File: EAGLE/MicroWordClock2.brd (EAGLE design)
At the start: 20.3 x 20.3 mm, 20 parts, among them IC1 ATMEGA328P, IC2 DS1307SMD

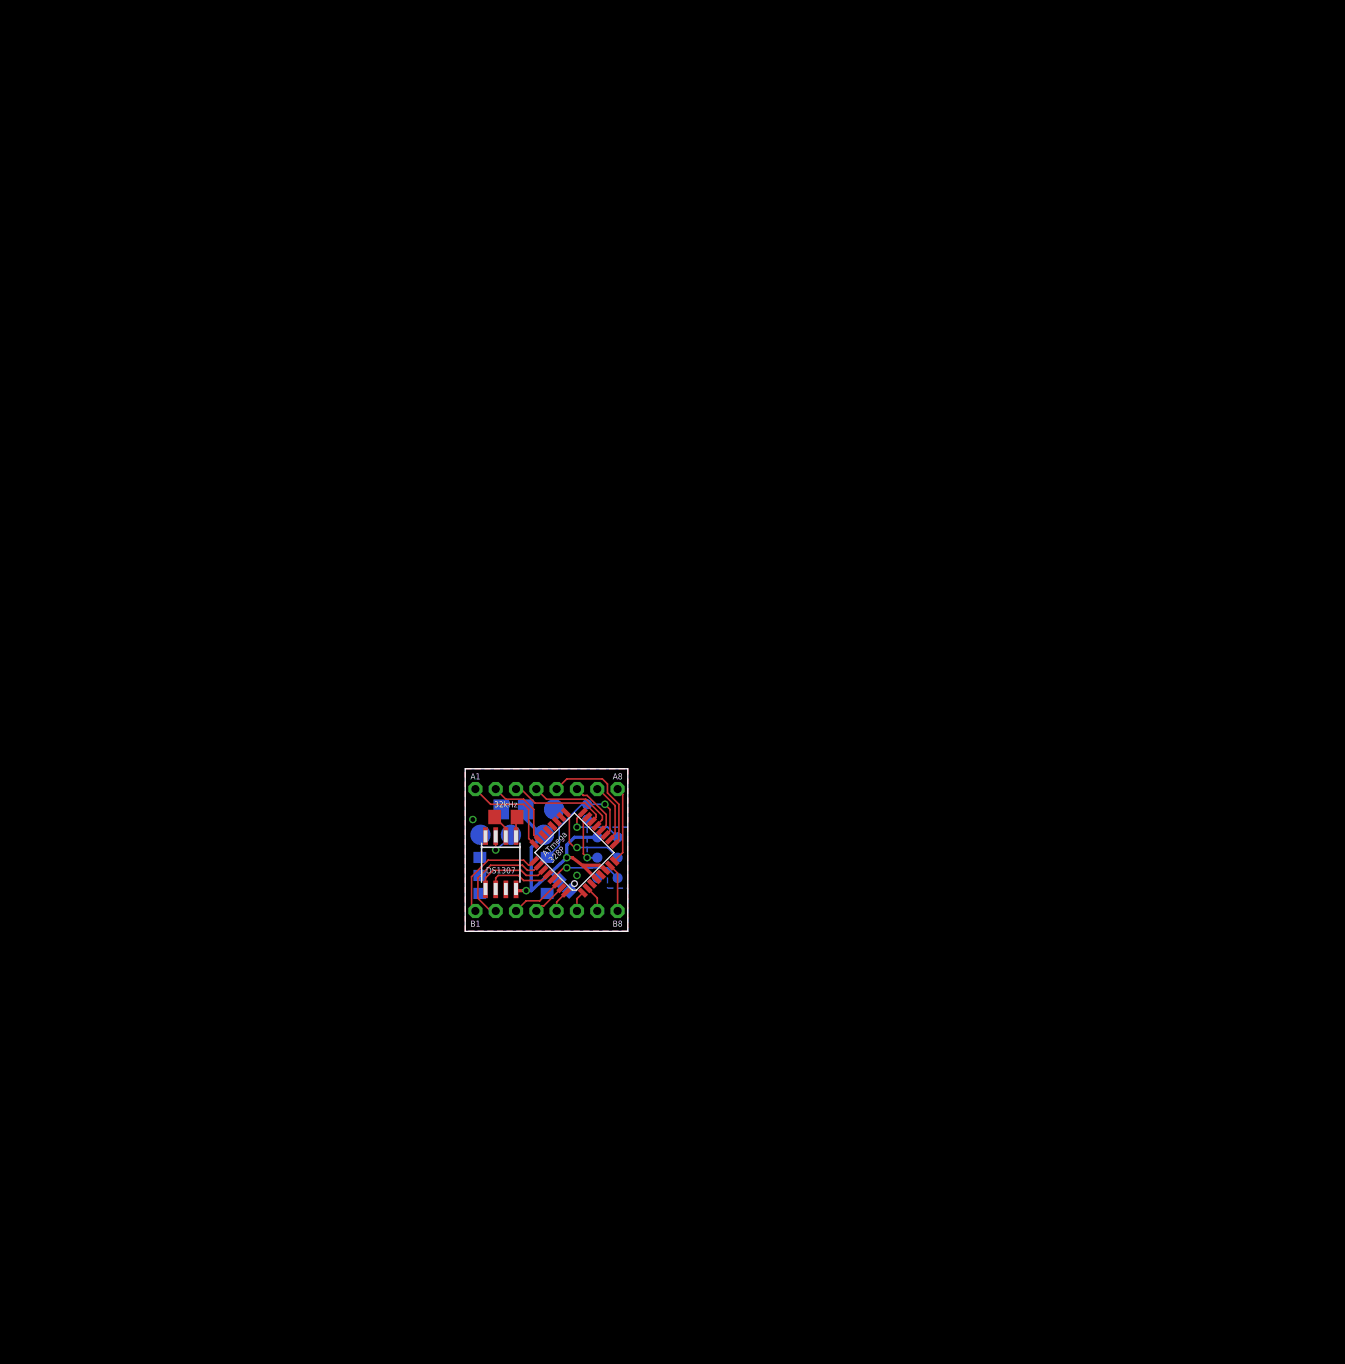
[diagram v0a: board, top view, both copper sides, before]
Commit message: initial edits to update the existing layout with the same components as the original
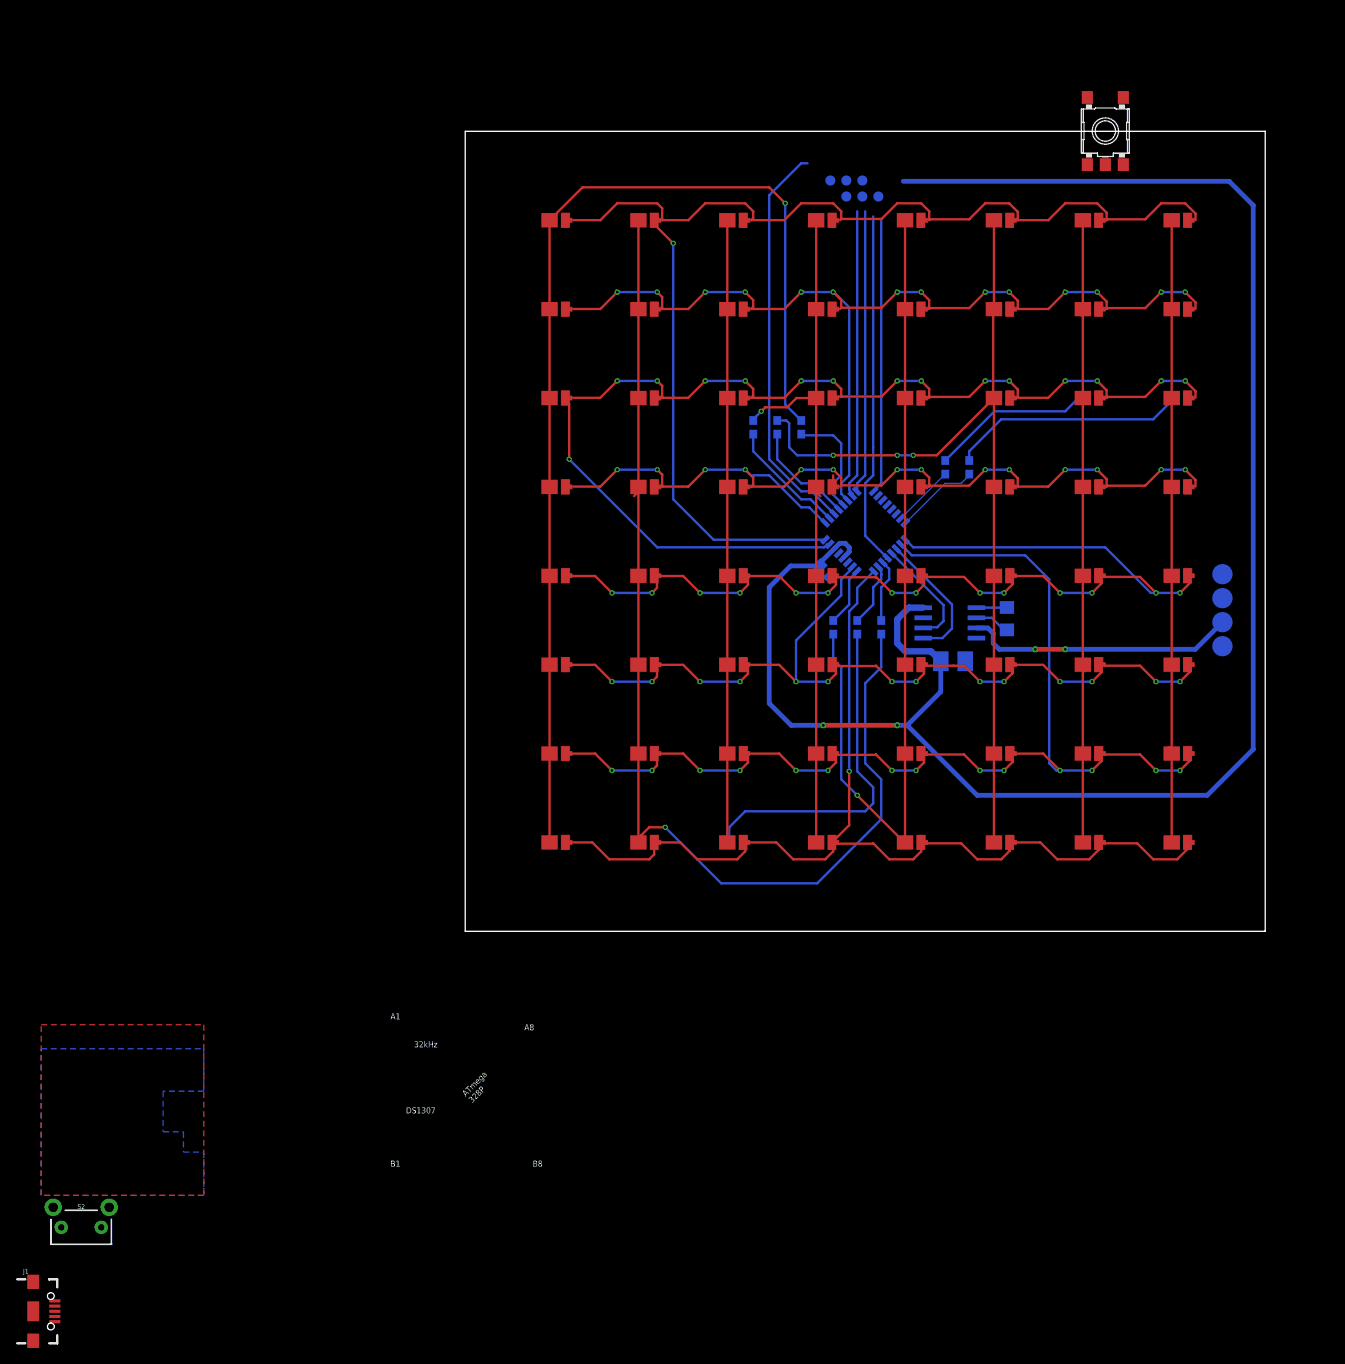
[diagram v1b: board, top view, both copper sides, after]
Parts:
- removed JP_A, JP_B: (no value), adafruit:1X08-CLEANBIG
- removed TP_SWITCH, TP_SWITCH_GND: TPB1,27, testpad:B1,27
- added J1: (no value), SparkFun-Connectors:USB-AB-MICRO-SMD
- added R1, R2, R3, R4, R5, R6, R7, R8: 470, SparkFun-Resistors:0603
- added S2: MOMENTARY-SWITCH-SPST-PTH-RIGHT-ANGLE-KIT, SparkFun-Switches:TACTILE_SWITCH_PTH_RIGHT_ANGLE_KIT
- added U$1, U$10, U$11, U$12, U$13, U$14, U$15, U$16, U$17, U$18, U$19, U$2, U$20, U$21, U$22, U$23, U$24, U$25, U$26, U$27, U$28, U$29, U$3, U$30, U$31, U$32, U$33, U$34, U$35, U$36, U$37, U$38, U$39, U$4, U$40, U$41, U$42, U$43, U$44, U$45, U$46, U$47, U$48, U$49, U$5, U$50, U$51, U$52, U$53, U$54, U$55, U$56, U$57, U$58, U$59, U$6, U$60, U$61, U$62, U$63, U$64, U$7, U$8, U$9: (no value), TULIP_GIZMO:1113(2835METRIC)
- moved S1 118.9 mm to (80.0, 100.0), flipped to the top, turned to 270 degrees
- moved TP_BAT- 95.7 mm to (94.7, 35.6), turned to 270 degrees
- moved TP_BAT+ 92.8 mm to (94.7, 38.6), turned to 270 degrees
- moved TP_GND 92.6 mm to (47.6, 93.8)
- moved TP_RST 89.9 mm to (47.6, 91.8)
- moved TP_VCC1 89.8 mm to (94.7, 41.6), turned to 270 degrees
- moved TP_MOSI 89.5 mm to (45.6, 93.8)
- moved TP_SCK 88.8 mm to (51.6, 91.8)
- moved TP_GND1 88.6 mm to (94.7, 44.6), turned to 270 degrees
- moved TP_MISO 87.6 mm to (49.6, 93.8)
- moved TP_VCC 86.7 mm to (49.6, 91.8)
- moved XTAL 67.4 mm to (67.7, 39.1), flipped to the bottom, turned to 90 degrees
- moved IC2 63.6 mm to (60.6, 38.6), flipped to the bottom, turned to 270 degrees
- moved C2 58.0 mm to (61.0, 33.8), turned to 0 degrees
- moved IC1 54.2 mm to (50.0, 50.0), flipped to the bottom
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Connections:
- removed net A1: IC1.24, JP_A.1
- removed net A2: IC1.23, JP_A.2
- removed net A3: IC1.14, JP_A.3
- removed net A4: IC1.13, JP_A.4
- removed net A5: IC1.9, JP_A.5
- removed net A6: IC1.12, JP_A.6
- removed net A7: IC1.10, JP_A.7
- removed net A8: IC1.8, JP_A.8
- removed net B1: IC1.25, JP_B.1
- removed net B2: IC1.26, JP_B.2
- removed net B3: IC1.30, JP_B.3
- removed net B4: IC1.31, JP_B.4
- removed net B5: IC1.32, JP_B.5
- removed net B6: IC1.1, JP_B.6
- removed net B7: IC1.2, JP_B.7
- removed net B8: IC1.7, JP_B.8
- new net COL1: IC1.13, R1.1
- new net COL2: IC1.30, R2.1
- new net COL3: IC1.31, R3.1
- new net COL4: IC1.10, R4.1
- new net COL5: IC1.1, R5.1
- new net COL6: IC1.12, R6.1
- new net COL7: IC1.23, R7.1
- new net COL8: IC1.24, R8.1
- new net EE: R8.2, U$57.CATHODE, U$58.CATHODE, U$59.CATHODE, U$60.CATHODE, U$61.CATHODE, U$62.CATHODE, U$63.CATHODE, U$64.CATHODE
- new net N$1: S1.1
- new net N$11: R1.2, U$1.CATHODE, U$2.CATHODE, U$3.CATHODE, U$4.CATHODE, U$5.CATHODE, U$6.CATHODE, U$7.CATHODE, U$8.CATHODE
- new net N$15: R2.2, U$10.CATHODE, U$11.CATHODE, U$12.CATHODE, U$13.CATHODE, U$14.CATHODE, U$15.CATHODE, U$16.CATHODE, U$9.CATHODE
- new net N$5: R3.2, U$17.CATHODE, U$18.CATHODE, U$19.CATHODE, U$20.CATHODE, U$21.CATHODE, U$22.CATHODE, U$23.CATHODE, U$24.CATHODE
- new net N$6: R4.2, U$25.CATHODE, U$26.CATHODE, U$27.CATHODE, U$28.CATHODE, U$29.CATHODE, U$30.CATHODE, U$31.CATHODE, U$32.CATHODE
- new net N$7: R5.2, U$33.CATHODE, U$34.CATHODE, U$35.CATHODE, U$36.CATHODE, U$37.CATHODE, U$38.CATHODE, U$39.CATHODE, U$40.CATHODE
- new net N$8: R6.2, U$41.CATHODE, U$42.CATHODE, U$43.CATHODE, U$44.CATHODE, U$45.CATHODE, U$46.CATHODE, U$47.CATHODE, U$48.CATHODE
- new net N$9: R7.2, U$49.CATHODE, U$50.CATHODE, U$51.CATHODE, U$52.CATHODE, U$53.CATHODE, U$54.CATHODE, U$55.CATHODE, U$56.CATHODE
- new net ROW1: IC1.8, U$1.ANODE, U$17.ANODE, U$25.ANODE, U$33.ANODE, U$41.ANODE, U$49.ANODE, U$57.ANODE, U$9.ANODE
- new net ROW2: IC1.14, U$10.ANODE, U$18.ANODE, U$2.ANODE, U$26.ANODE, U$34.ANODE, U$42.ANODE, U$50.ANODE, U$58.ANODE
- new net ROW3: IC1.7, U$11.ANODE, U$19.ANODE, U$27.ANODE, U$3.ANODE, U$35.ANODE, U$43.ANODE, U$51.ANODE, U$59.ANODE
- new net ROW4: IC1.9, U$12.ANODE, U$20.ANODE, U$28.ANODE, U$36.ANODE, U$4.ANODE, U$44.ANODE, U$52.ANODE, U$60.ANODE
- new net ROW5: IC1.25, U$13.ANODE, U$21.ANODE, U$29.ANODE, U$37.ANODE, U$45.ANODE, U$5.ANODE, U$53.ANODE, U$61.ANODE
- new net ROW6: IC1.2, U$14.ANODE, U$22.ANODE, U$30.ANODE, U$38.ANODE, U$46.ANODE, U$54.ANODE, U$6.ANODE, U$62.ANODE
- new net ROW7: IC1.26, U$15.ANODE, U$23.ANODE, U$31.ANODE, U$39.ANODE, U$47.ANODE, U$55.ANODE, U$63.ANODE, U$7.ANODE
- new net ROW8: IC1.32, U$16.ANODE, U$24.ANODE, U$32.ANODE, U$40.ANODE, U$48.ANODE, U$56.ANODE, U$64.ANODE, U$8.ANODE
- new net VBUS: J1.VBUS1
- net GND: now also J1.GND1, J1.SHLD1, J1.SHLD2, J1.SHLD3; no longer TP_SWITCH_GND.TP
- net SWITCH: no longer S1.1, TP_SWITCH.TP
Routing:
- net +5V: track 37.0 -> 232.4 mm
- net ROW1: track 0.00 -> 150.8 mm, vias 0 -> 1
- net N$15: track 0.00 -> 142.4 mm, vias 0 -> 1
- net ROW3: track 0.00 -> 140.1 mm, vias 0 -> 15
- net ROW7: track 0.00 -> 140.0 mm, vias 0 -> 14
- net N$11: track 0.00 -> 137.8 mm, vias 0 -> 1
- net ROW8: track 0.00 -> 131.0 mm, vias 0 -> 1
- net ROW5: track 0.00 -> 129.0 mm, vias 0 -> 14
- net ROW2: track 0.00 -> 122.5 mm, vias 0 -> 14
- net N$5: track 0.00 -> 122.3 mm
- net ROW6: track 0.00 -> 112.1 mm, vias 0 -> 14
- net N$8: track 0.00 -> 110.5 mm, vias 0 -> 3
- net ROW4: track 0.00 -> 109.1 mm, vias 0 -> 14
- net EE: track 0.00 -> 108.7 mm
- net N$7: track 0.00 -> 107.2 mm, vias 0 -> 1
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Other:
- board size 20.3 x 20.3 mm -> 100 x 100 mm

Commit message: board with new footprints for switch, microusb and clock & complete routing
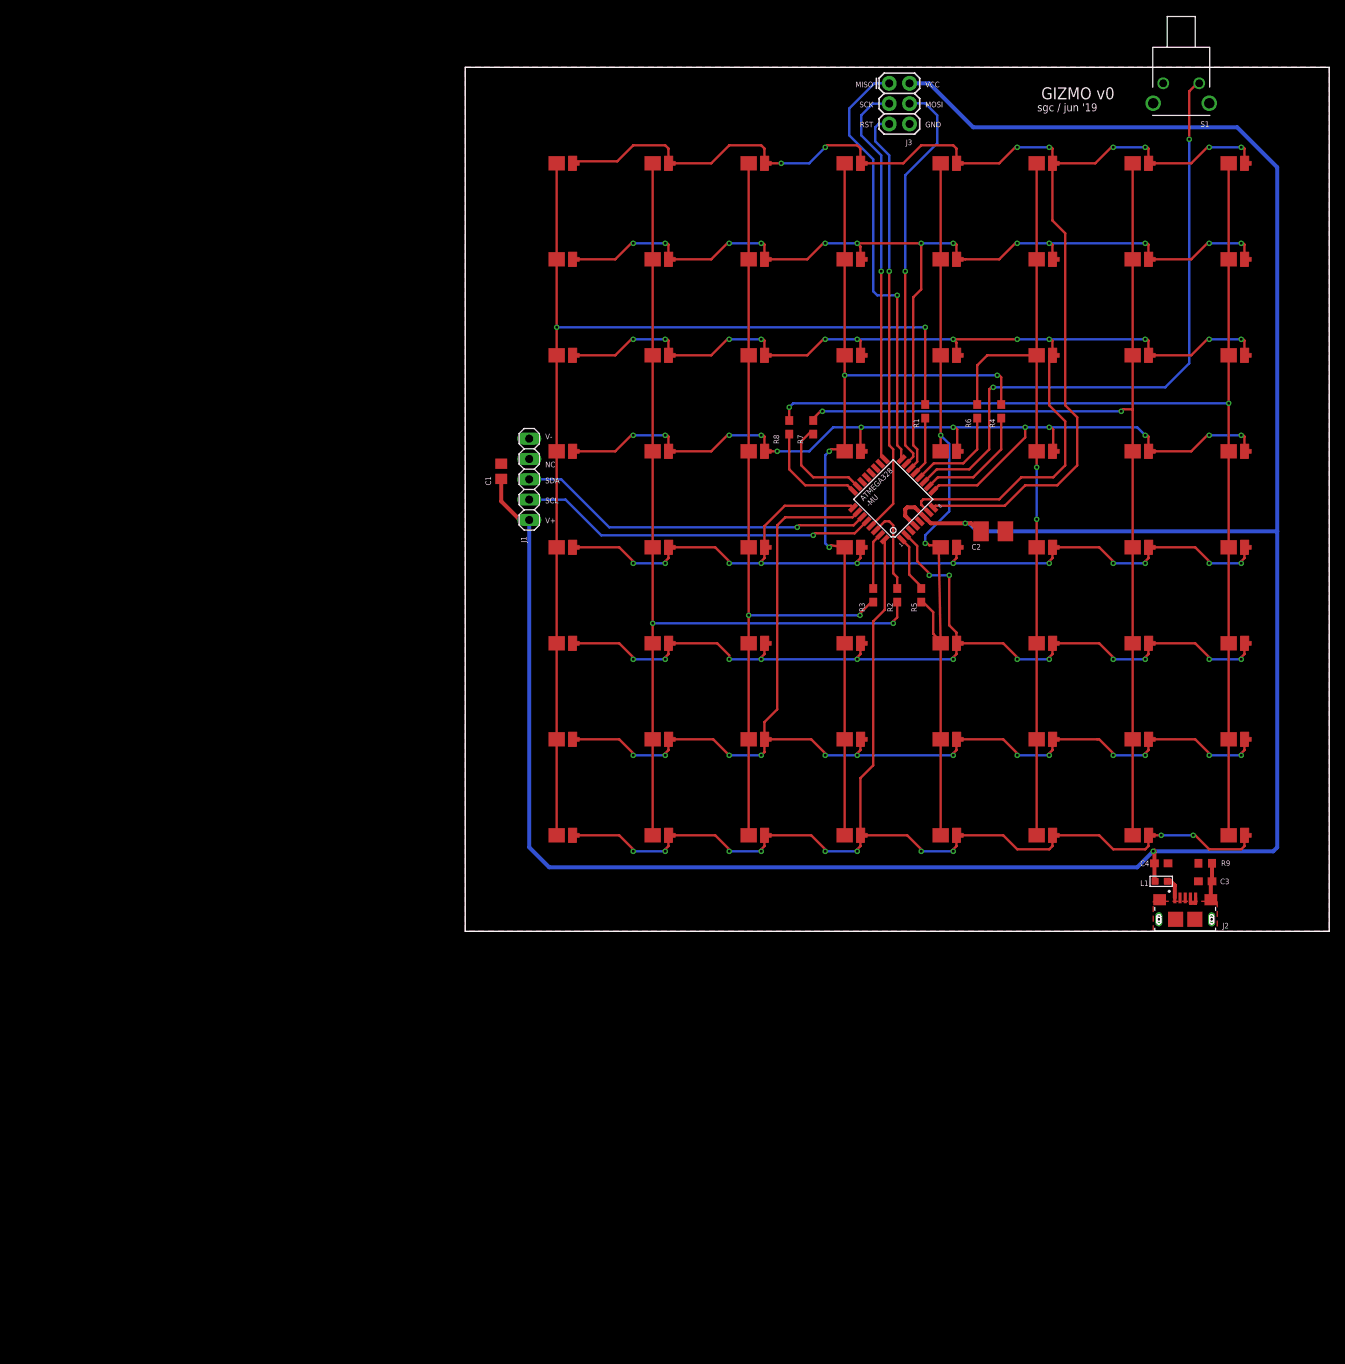
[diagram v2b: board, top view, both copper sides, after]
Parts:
- removed IC1: ATMEGA328P, atmel:TQFP32-08
- removed IC2: DS1307SMD, DS1307:SO-08M
- removed S2: MOMENTARY-SWITCH-SPST-PTH-RIGHT-ANGLE-KIT, SparkFun-Switches:TACTILE_SWITCH_PTH_RIGHT_ANGLE_KIT
- removed TP_BAT+, TP_BAT-, TP_GND1, TP_VCC1: TPB2,54, testpad:B2,54
- removed TP_GND, TP_MISO, TP_MOSI, TP_RST, TP_SCK, TP_VCC: TPB1,27, testpad:B1,27
- removed XTAL: XTAL-32KHZ, xtal-32khz:XTAL-SMD-1206-3216M
- added C3: 4700pF, rcl:C0603
- added C4: 4.7uF, rcl:C0603
- added J2: 10118193-0001LF, 10118193-0001LF:FCI_10118193-0001LF
- added J3: AVR_SPI_PROG_3X2PTH, SparkFun-Connectors:2X3
- added L1: 120OHM-500MA, OPL_Ferrite_and_Magnetic_Bead:L0603
- added R9: 10M, rcl:R0603
- added U1: ATMEGA328P, atmel:TQFP32-08
- J1: value (none) -> DS3231S#T&RMODULE; device SparkFun-Connectors:USB-AB-MICRO-SMD -> DS3231:1X05
- S1: value SKHMPSE010 -> 1-1825027-1; device switch:SKHMPXE010 -> 1-1825027-1:SW_1-1825027-1
- moved J1 121.1 mm to (8.00, 56.5), turned to 90 degrees
- moved C1 42.4 mm to (4.50, 57.5), flipped to the top, turned to 90 degrees
- moved R4 31.1 mm to (67.0, 65.0), flipped to the top
- moved R6 25.1 mm to (64.0, 65.0), flipped to the top
- moved R8 23.0 mm to (40.5, 63.0), flipped to the top
- moved R7 17.2 mm to (43.5, 63.0), flipped to the top
- moved C2 17.0 mm to (66.0, 50.0), flipped to the top, turned to 180 degrees
- moved R1 15.6 mm to (57.5, 65.0), flipped to the top
- moved R5 11.7 mm to (57.0, 42.0), flipped to the top
- moved S1 11.2 mm to (89.5, 106.0), turned to 180 degrees
- moved U$57 10.1 mm to (96.0, 96.0)
- moved U$49 9.46 mm to (84.0, 96.0)
- moved U$58 9.46 mm to (96.0, 84.0)
- moved U$41 8.90 mm to (72.0, 96.0)
- moved U$59 8.90 mm to (96.0, 72.0)
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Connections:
- removed net N$14: IC2.1, XTAL.X2
- removed net N$18: IC1.28, IC2.6
- removed net N$2: IC2.2, XTAL.X1
- removed net SWITCH: IC1.11
- removed net VBAT: IC2.3, TP_BAT+.TP
- removed net VBUS: J1.VBUS1
- new net PE: C3.2, J2.S1, J2.S2, J2.S3, J2.S4, J2.S5, J2.S6, R9.1
- new net SCL: J1.2, U1.28
- new net V_USB: J2.1, L1.1
- net +5V: now also C4.1, J1.1, J3.2, L1.2, U1.4, U1.6; no longer IC1.4, IC1.6, IC2.8, TP_VCC.TP, TP_VCC1.TP
- net AVCC: now also U1.18; no longer IC1.18
- net COL1: now also U1.13; no longer IC1.13
- net COL2: now also U1.30; no longer IC1.30
- net COL3: now also U1.31; no longer IC1.31
- net COL4: now also U1.10; no longer IC1.10
- net COL5: now also U1.1; no longer IC1.1
- net COL6: now also U1.12; no longer IC1.12
- net COL7: now also U1.23; no longer IC1.23
- net COL8: now also U1.24; no longer IC1.24
- net GND: now also C3.1, C4.2, J1.5, J2.4, J2.5, J3.6, R9.2, S1.2, S1.S1, S1.S2, U1.21, U1.3, U1.5; no longer IC1.21, IC1.3, IC1.5, IC2.4, J1.GND1, J1.SHLD1, J1.SHLD2, J1.SHLD3, S1.3, S1.4, S1.5, TP_BAT-.TP, TP_GND.TP, TP_GND1.TP
- net MISO: now also J3.1, U1.16; no longer IC1.16, TP_MISO.TP
- net MOSI: now also J3.4, U1.15; no longer IC1.15, TP_MOSI.TP
- net N$1: now also U1.11
- net RESET: now also J3.5, U1.29; no longer IC1.29, TP_RST.TP
- net ROW1: now also U1.8; no longer IC1.8
- net ROW2: now also U1.14; no longer IC1.14
- net ROW3: now also U1.7; no longer IC1.7
- net ROW4: now also U1.9; no longer IC1.9
- net ROW5: now also U1.25; no longer IC1.25
- net ROW6: now also U1.2; no longer IC1.2
- net ROW7: now also U1.26; no longer IC1.26
- net ROW8: now also U1.32; no longer IC1.32
- net SCK: now also J3.3, U1.17; no longer IC1.17, TP_SCK.TP
- net SDA: now also J1.3, U1.27; no longer IC1.27, IC2.5
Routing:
- net +5V: track 232.4 -> 336.0 mm
- net N$1: track 0.00 -> 79.3 mm, vias 0 -> 2
- net SWITCH: track 50.4 -> 0.00 mm
- net SCL: track 0.00 -> 44.8 mm, vias 0 -> 1
- net VBAT: track 34.0 -> 0.00 mm, vias 2 -> 0
- net EE: track 108.7 -> 140.8 mm, vias 0 -> 2
- net SDA: track 17.0 -> 44.6 mm, vias 0 -> 1
- net N$15: track 142.4 -> 116.9 mm, vias 1 -> 2
- net N$9: track 100.6 -> 124.7 mm, vias 0 -> 2
- net N$6: track 88.2 -> 111.3 mm, vias 1 -> 4
- net N$5: track 122.3 -> 100.4 mm, vias 0 -> 2
- net MISO: track 35.4 -> 54.3 mm, vias 0 -> 1
- net MOSI: track 36.1 -> 50.1 mm, vias 0 -> 1
- net SCK: track 34.4 -> 48.3 mm, vias 0 -> 1
- net N$8: track 110.5 -> 96.8 mm, vias 3 -> 2
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- added copper zone on layer 1, net PE
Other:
- board size 100 x 100 mm -> 108 x 108 mm
- board text added: "1"
- board text added: "8"
- board text added: "ATMEGA328 -MU"
- board text added: "GIZMO v0"
- board text added: "MISO"
- board text added: "MOSI"
- board text added: "NC"
- board text added: "RST"
- board text added: "SCK"
- board text added: "SCL"
- board text added: "SDA"
- board text added: "V+"
- board text added: "V-"
- board text added: "sgc / jun '19"
- board text removed: "+"
- board text removed: "-"
- board text removed: "2.2 uF"
- board text removed: "32kHz"
- board text removed: "A1"
- board text removed: "A8"
- board text removed: "ATmega 328P"
- board text removed: "B1"
- board text removed: "B8"
- board text removed: "BAT"
- board text removed: "DS1307"
- board text removed: "Daniel Rojas 06/2014"
- board text removed: "ICSP"
- board text removed: "MicroWordClock v2"
- board text removed: "SET"

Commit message: fixing some stray wires, adding the tulip logo to the back
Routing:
- net ROW1: track 163.6 -> 163.2 mm, vias 8 -> 10
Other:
- board text added: "/Users/samchin/Downloads/Tulip Logo Flower (1).bmp"
